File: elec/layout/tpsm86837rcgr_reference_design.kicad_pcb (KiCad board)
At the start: 2 copper layers, 7 parts

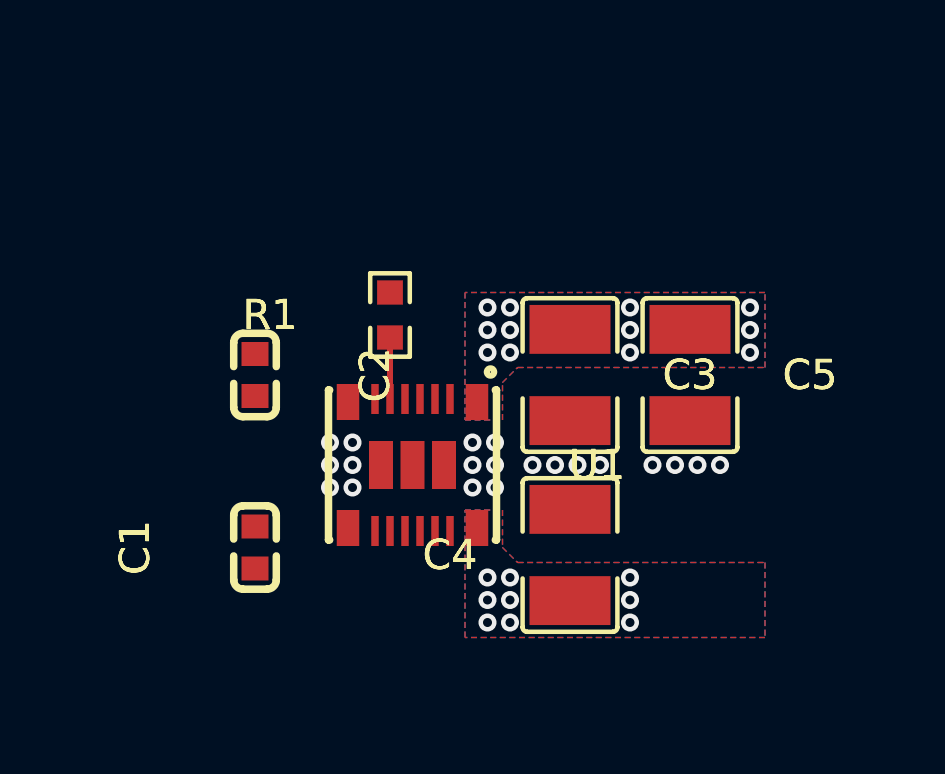
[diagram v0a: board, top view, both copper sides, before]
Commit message: Change PCB layout
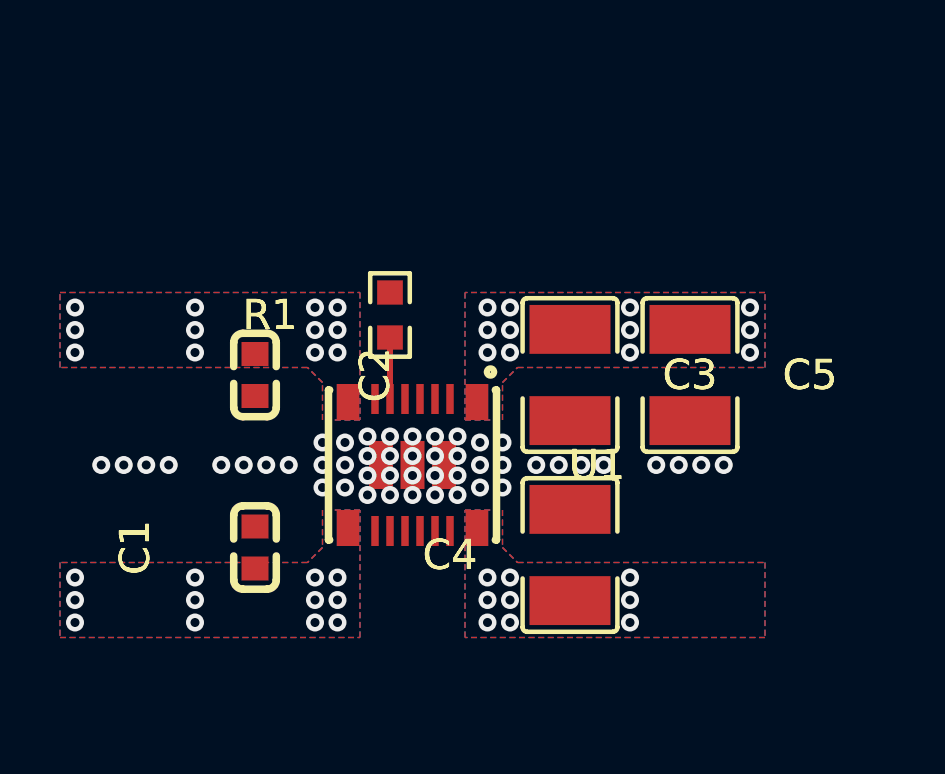
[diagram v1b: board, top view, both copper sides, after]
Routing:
- net hv-1: vias 0 -> 24
- net gnd: vias 0 -> 20
- net (no net): vias 20 -> 28
- added copper zone on B.Cu, net hv-1
- added copper zone on F.Cu, net hv-1

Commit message: Add LED buffer, change DCDC func to params, layout
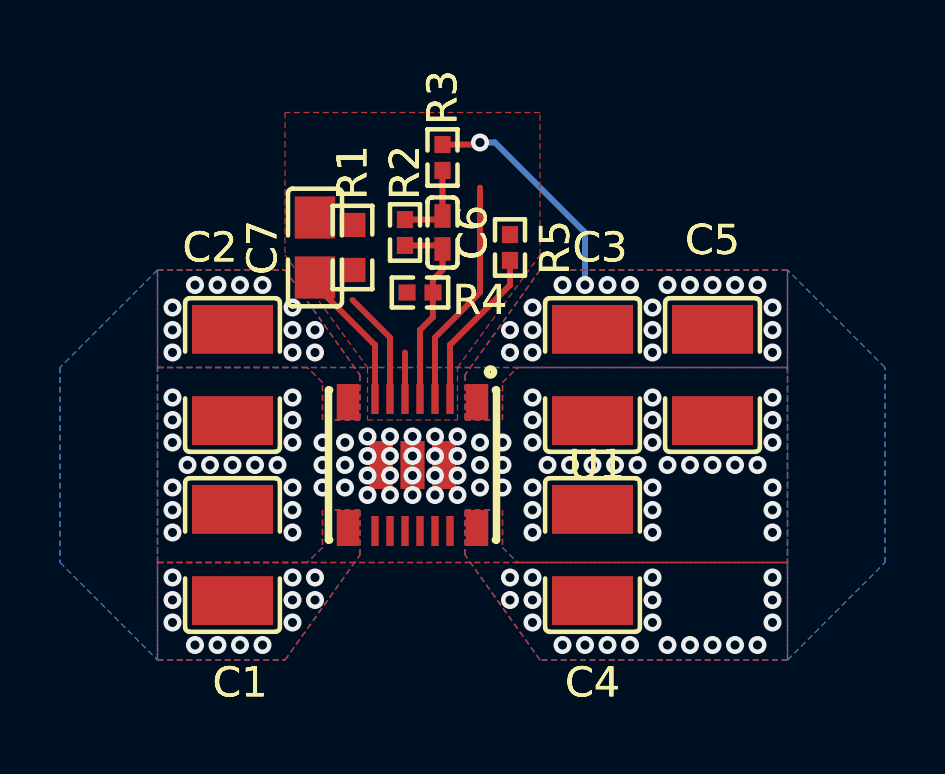
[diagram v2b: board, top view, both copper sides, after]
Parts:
- added C6: 47pF ±1%, atopile:C0402-b3ef17, F.Cu at (1.00, -7.75)
- added C7: 22nF ±1% 50V, atopile:C0805-3b2e55, F.Cu at (-3.25, -7.25)
- added R2: 1kΩ ±1% 62.5mW, atopile:R0402-56259e, F.Cu at (-0.25, -7.75)
- added R3: 49.9Ω ±1% 62.5mW, atopile:R0402-56259e, F.Cu at (1.00, -10.2)
- added R4: 10kΩ ±1% 62.5mW, atopile:R0402-56259e, F.Cu at (0.25, -5.75)
- added R5: 374kΩ ±1% 100mW, atopile:R0402-56259e, F.Cu at (3.25, -7.25)
- C1, C2: value 10µF ±10% 10V X5R -> 10µF ±10% 35V X7R; footprint atopile:C0603-bd72f6 -> atopile:C1210-c93926
- moved R1 2.57 mm to (-2.00, -7.25)
- moved C1 0.79 mm to (-6.00, 3.00)
- moved C2 0.75 mm to (-6.00, -3.00)
- moved C3 0.75 mm to (6.00, -3.00)
- moved C4 0.75 mm to (6.00, 3.00)
- moved C5 0.75 mm to (10.0, -3.00)
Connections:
- net gnd renamed gnd-2
- net signal renamed line-2
- net signal-1 renamed line
- U1 pad 4: feedback -> line-1
- U1 pad 5: power_module-gnd -> gnd-1
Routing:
- net hv: track 0.00 -> 7.77 mm, vias 21 -> 41
- net line: track 0.00 -> 7.67 mm
- net line-1: track 0.00 -> 6.61 mm
- net frequency_mode: track 0.00 -> 5.45 mm
- net soft_start: track 0.00 -> 4.63 mm
- net output_voltage_feedback-hv: track 0.00 -> 2.82 mm
- net line-2: track 2.05 -> 3.82 mm
- net gnd-1: track 0.00 -> 1.55 mm
- net gnd-2: vias 20 -> 77
- net (no net): vias 28 -> 0
- added copper zone on F.Cu, net gnd-1
- added copper zone on B.Cu, net gnd-2
- added copper zone on F.Cu, net gnd-2

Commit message: Add pcb files
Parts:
- added JP1: , NetTie:NetTie-2_SMD_Pad0.5mm, F.Cu at (-4.25, -11.0)
- added TP1: , TestPoint:TestPoint_Pad_D1.0mm, B.Cu at (3.50, -10.0)
- added TP2: , TestPoint:TestPoint_Pad_D1.0mm, B.Cu at (-0.25, -10.0)
- C6: value 47pF ±1% -> 47pF ±1% 50V C0G
- C7: value 22nF ±1% 50V -> 22nF ±10% 50V X7R; footprint atopile:C0805-3b2e55 -> atopile:C0402-b3ef17
- R1: value 100kΩ ±1% 100mW -> 100kΩ ±1% 62.5mW; footprint atopile:R0603-ebcab9 -> atopile:R0402-56259e
- R2: value 1kΩ ±1% 62.5mW -> 10kΩ ±1% 62.5mW
- R5: value 374kΩ ±1% 100mW -> 10kΩ ±1% 100mW; footprint atopile:R0402-56259e -> atopile:R0603-ebcab9
- moved R2 2.06 mm to (0.25, -5.75), turned to 180 degrees
- moved R4 2.06 mm to (-0.25, -7.75), turned to -90 degrees
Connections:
- C1 pad 1: hv-1 -> hv
- C1 pad 2: gnd-2 -> gnd-1
- C2 pad 1: hv-1 -> hv
- C2 pad 2: gnd-2 -> gnd-1
- C3 pad 1: hv -> hv-1
- C3 pad 2: gnd-2 -> gnd-1
- C4 pad 1: hv -> hv-1
- C4 pad 2: gnd-2 -> gnd-1
- C5 pad 1: hv -> hv-1
- C5 pad 2: gnd-2 -> gnd-1
- C6 pad 2: output_voltage_feedback-hv -> output_voltage_feedback-contact
- C7 pad 2: gnd-1 -> gnd
- R1 pad 1: line-2 -> line
- R2 pad 1: output_voltage_feedback-hv -> line-1
- R2 pad 2: line-1 -> gnd
- R3 pad 1: hv -> output_voltage_feedback-contact-1
- R3 pad 2: output_voltage_feedback-hv -> output_voltage_feedback-contact
- R4 pad 1: line-1 -> output_voltage_feedback-contact
- R4 pad 2: gnd -> line-1
- R5 pad 2: gnd-1 -> gnd
- U1 pad 1: hv -> hv-1
- U1 pad 13: gnd-2 -> gnd-1
- U1 pad 14: gnd-2 -> gnd-1
- U1 pad 15: gnd-2 -> gnd-1
- U1 pad 16: hv -> hv-1
- U1 pad 17: gnd-2 -> gnd-1
- U1 pad 18: gnd-2 -> gnd-1
- U1 pad 19: gnd-2 -> gnd-1
- U1 pad 3: line -> line-2
- U1 pad 5: gnd-1 -> gnd
- U1 pad 6: line-2 -> line
- U1 pad 8: hv-1 -> hv
- U1 pad 9: hv-1 -> hv
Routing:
- net output_voltage_feedback-contact-1: track 0.00 -> 7.77 mm, vias 0 -> 2
- net hv: track 7.77 -> 0.00 mm, vias 41 -> 24
- net output_voltage_feedback-contact: track 0.00 -> 4.19 mm, vias 0 -> 1
- net output_voltage_feedback-hv: track 2.82 -> 0.00 mm
- net line: track 7.67 -> 5.14 mm
- net line-2: track 3.82 -> 6.17 mm
- net gnd-1: track 1.55 -> 0.00 mm, vias 0 -> 77
- net gnd: track 0.00 -> 1.55 mm
- net soft_start: track 4.63 -> 5.33 mm
- net hv-1: vias 24 -> 39
- net gnd-2: vias 77 -> 0
- added copper zone on F.Cu, net gnd
- added copper zone on B.Cu, net gnd-1
- removed copper zone on B.Cu, net gnd-2
- removed copper zone on F.Cu, net gnd-2
